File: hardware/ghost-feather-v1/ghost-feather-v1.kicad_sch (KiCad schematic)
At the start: 41 parts, among them J1 Conn_ARM_SWD_TagConnect_TC2030, J2 USB_C_Receptacle_USB2.0, J3 Conn_01x03, J4 Conn_01x03, J5 Conn_01x03, J6 Conn_01x03, SW2 BOOT0, U1 STM32F722RETx, U2 BMI270, U3 USBLC6-2SC6_MOD, U4 ADP2108AUJ-3.3, U5 LM2596S-5, X2 32kHz768

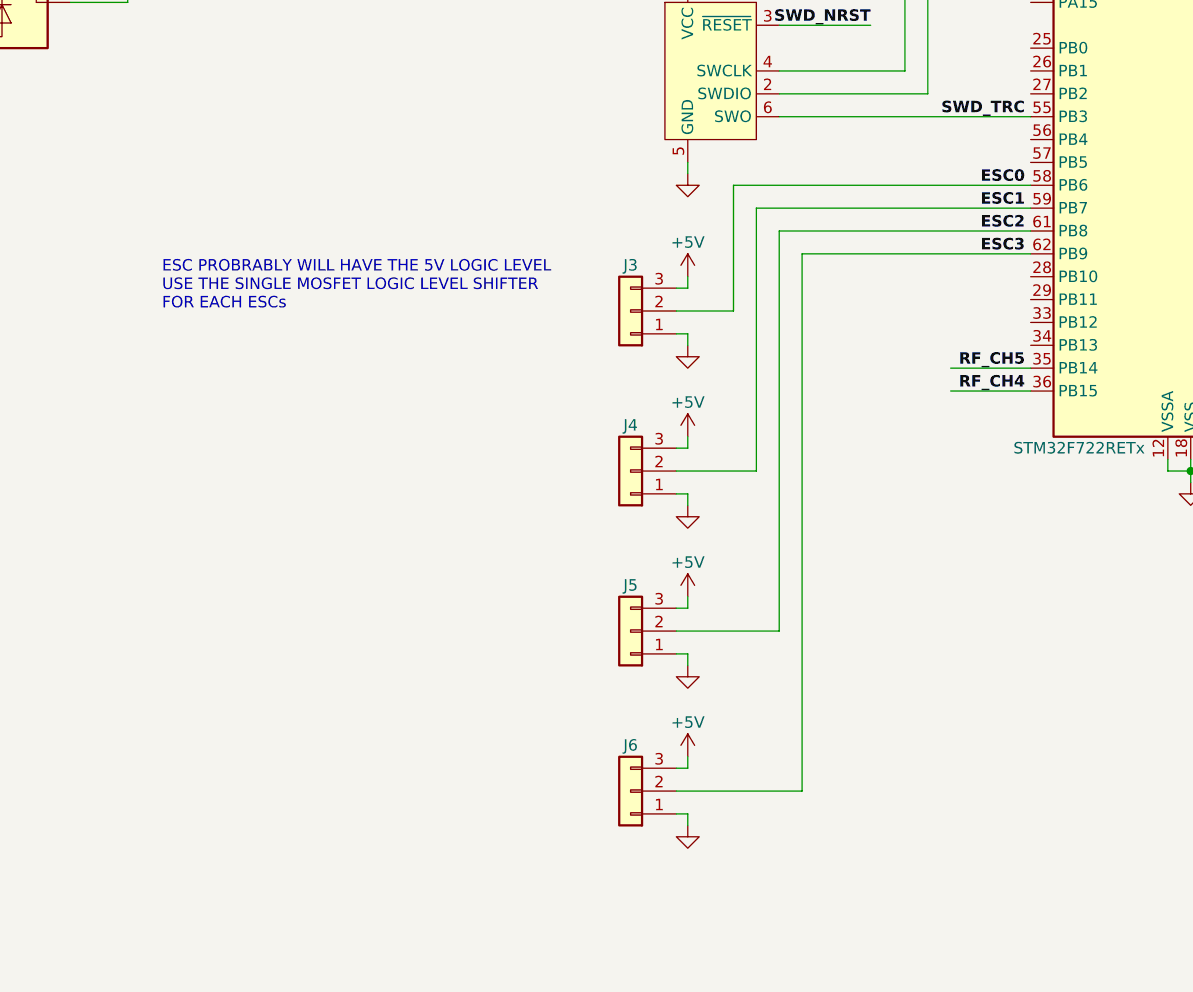
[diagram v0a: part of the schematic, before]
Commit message: feat: Add the MOSFET logic level shifters for every ESC
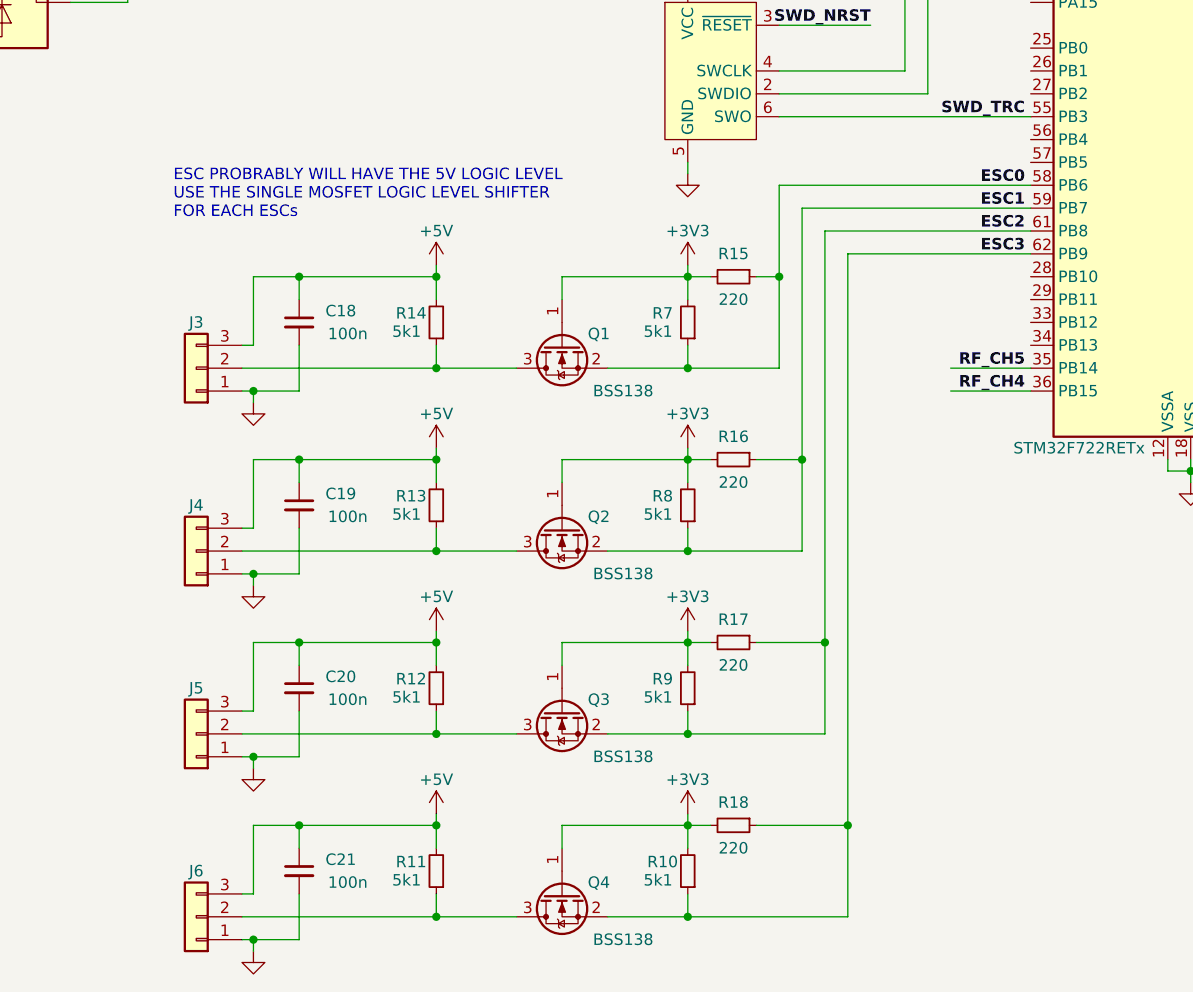
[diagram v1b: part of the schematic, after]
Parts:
- added C18, C19, C20, C21: 100n, symbol Device:C_Small
- added Q1, Q2, Q3, Q4: BSS138, Package_TO_SOT_SMD:SOT-23, symbol Transistor_FET:BSS138
- added R10, R11, R12, R13, R14, R7, R8, R9: 5k1, symbol Device:R_Small
- added R15, R16, R17, R18: 220, symbol Device:R_Small
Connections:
- net +3V3: now also Q1.1 (G), Q2.1 (G), Q3.1 (G), Q4.1 (G), R10.2, R15.2, R16.2, R17.2, R18.2, R7.2, R8.2, R9.2
- net +5V: now also C18.1, C19.1, C20.1, C21.1, R11.2, R12.2, R13.2, R14.2
- net ESC0: now also Q1.2 (S), R15.1, R7.1; no longer J3.2 (Pin_2)
- net ESC1: now also Q2.2 (S), R16.1, R8.1; no longer J4.2 (Pin_2)
- net ESC2: now also Q3.2 (S), R17.1, R9.1; no longer J5.2 (Pin_2)
- net ESC3: now also Q4.2 (S), R10.1, R18.1; no longer J6.2 (Pin_2)
- net GND: now also C18.2, C19.2, C20.2, C21.2
- new net: J5.2 (Pin_2), Q3.3 (D), R12.1
- new net: J3.2 (Pin_2), Q1.3 (D), R14.1
- new net: J4.2 (Pin_2), Q2.3 (D), R13.1
- new net: J6.2 (Pin_2), Q4.3 (D), R11.1
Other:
- moved on the sheet: J3, J4, J5, J6

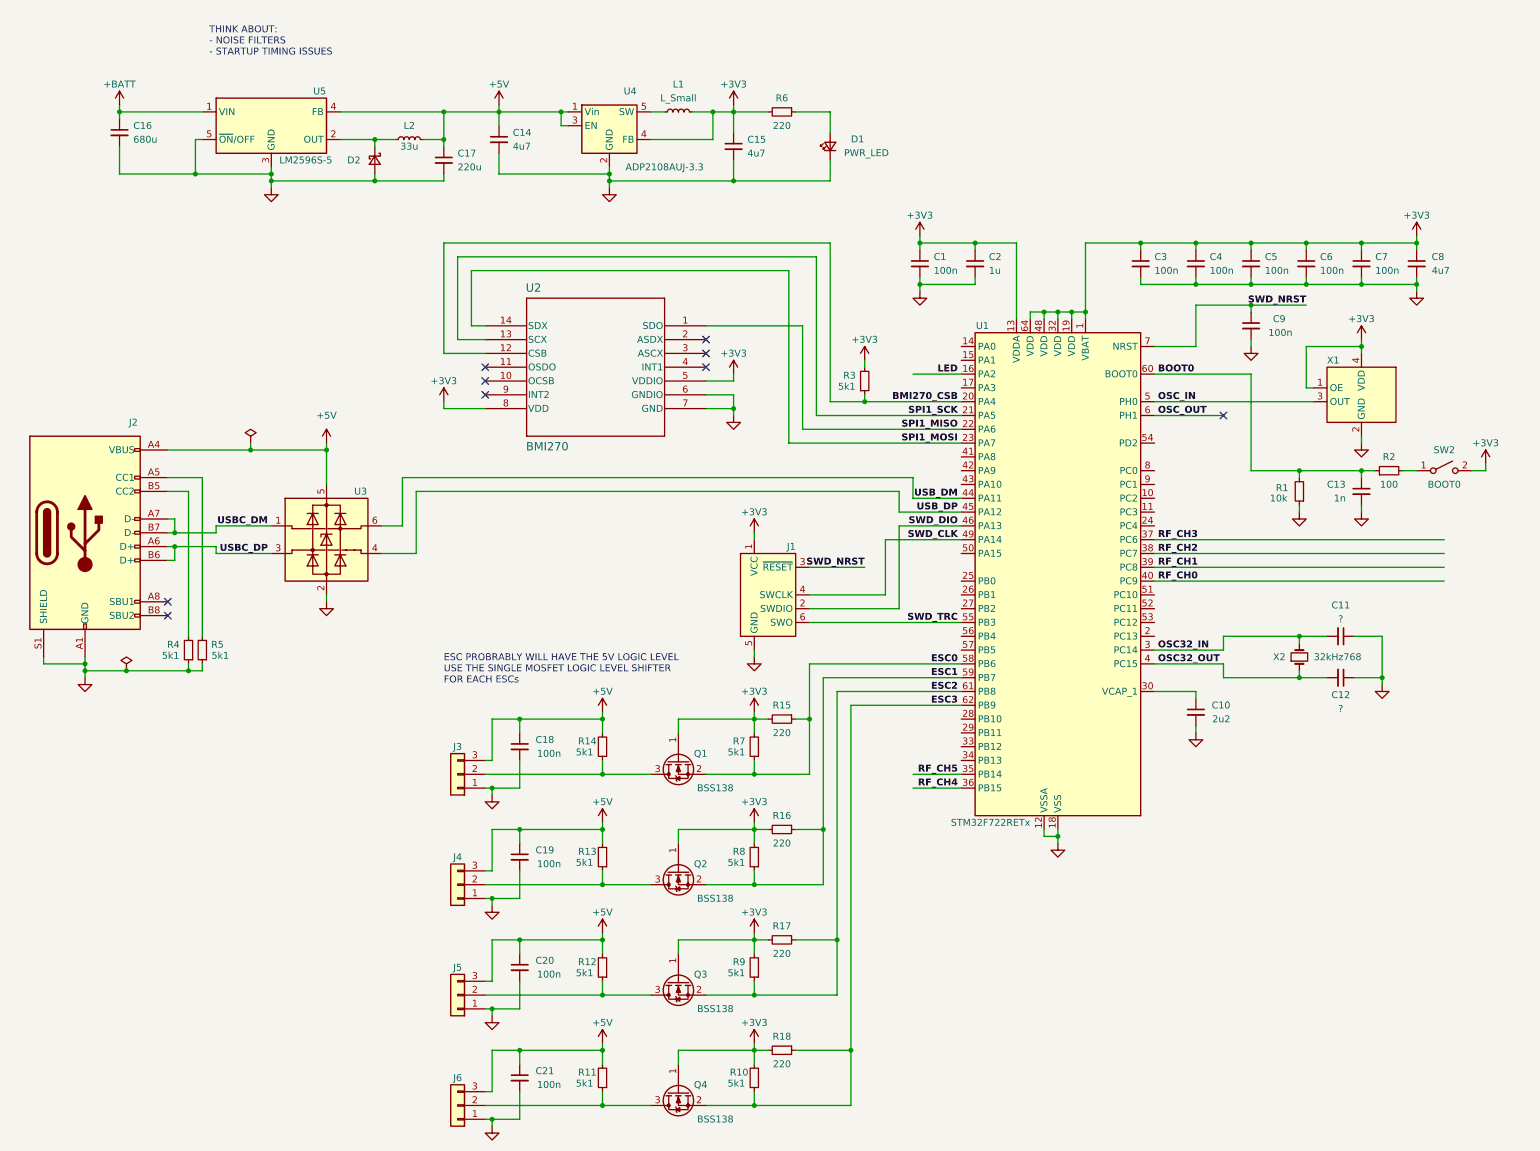
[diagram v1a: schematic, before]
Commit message: feat: Add RF channel connector. Start adding the parts information
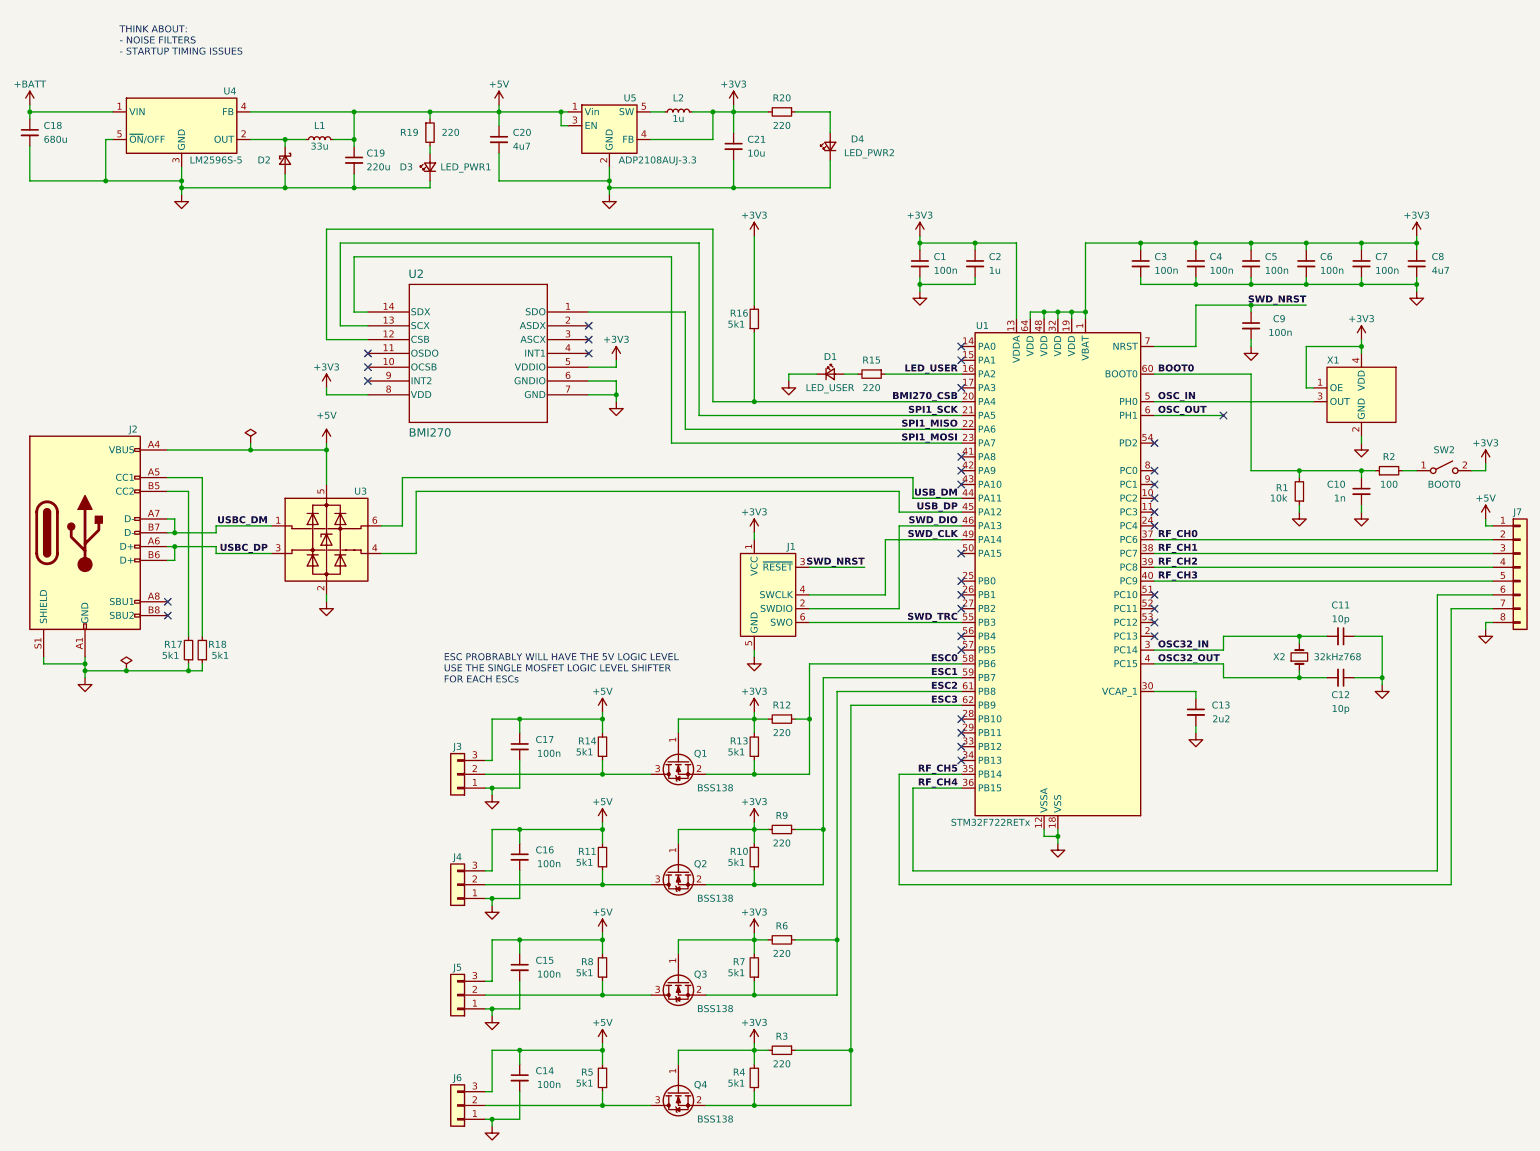
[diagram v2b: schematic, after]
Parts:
- removed R3: 5k1, symbol Device:R_Small
- added D1: LED_USER, symbol Device:LED_Small
- added D3: LED_PWR1, symbol Device:LED_Small
- added J7: Conn_01x08, symbol Connector_Generic:Conn_01x08
- added R15, R19: 220, symbol Device:R_Small
- added R16: 5k1, symbol Device:R_Small
- C11, C12: value ? -> 10p
- C21: renamed from C15; value 4u7 -> 10u
- D4: renamed from D1; value PWR_LED -> LED_PWR2
- L2: renamed from L1; value L_Small -> 1u
- U1: Distributor Link (none) -> https://eu.mouser.com/ProductDetail/STMicroelectronics/STM3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; Manufacturer (none) -> STMicroelectronics; Manufacturer Part Number (none) -> STM32F722RET6
- U2: Distributor Link (none) -> https://eu.mouser.com/ProductDetail/Bosch-Sensortec/BMI270?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; Manufacturer (none) -> Bosch Sensortec; Manufacturer Part Number (none) -> BMI270
- U3: Distributor Link (none) -> https://eu.mouser.com/ProductDetail/STMicroelectronics/USBL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; Manufacturer (none) -> STMicroelectronics; Manufacturer Part Number (none) -> USBLC6-2SC6
- U4: renamed from U5; Distributor Link (none) -> https://eu.mouser.com/ProductDetail/Texas-Instruments/LM259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; Manufacturer (none) -> Texas Instruments; Manufacturer Part Number (none) -> LM2596S-5.0/NOPB
- U5: renamed from U4; Distributor Link (none) -> https://eu.mouser.com/ProductDetail/Analog-Devices/ADP2108A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; Manufacturer (none) -> Analog Devices; Manufacturer Part Number (none) -> ADP2108AUJZ-3.3-R7
- X1: Distributor Link (none) -> https://eu.mouser.com/ProductDetail/ABRACON/AMPMGFB-16.0000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; Manufacturer (none) -> ABRACON; Manufacturer Part Number (none) -> AMPMGFB-16.0000T
- X2: Distributor Link (none) -> https://eu.mouser.com/ProductDetail/Micro-Crystal/CC4V-T1A-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; Manufacturer (none) -> Micro Crystal; Manufacturer Part Number (none) -> CC4V-T1A-32.768kHz-10pF-20PPM-TA-QC
- renumbered C13 to C10, C10 to C13, C21 to C14, C20 to C15, C19 to C16, C18 to C17, C16 to C18, C17 to C19, C14 to C20, L2 to L1, R8 to R10, R13 to R11, R15 to R12, R7 to R13, R4 to R17, R5 to R18, R6 to R20, R18 to R3, R10 to R4, R11 to R5, R17 to R6, R9 to R7, R12 to R8, R16 to R9
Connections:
- net +3V3: now also R16.2
- net +5V: now also J7.1 (Pin_1), R19.1
- net BMI270_CSB: now also R16.1
- net GND: now also D1.1 (K), D3.1 (K), J7.8 (Pin_8)
- net RF_CH0: now also U1.37 (PC6), J7.2 (Pin_2); no longer U1.40 (PC9)
- net RF_CH1: now also U1.38 (PC7), J7.3 (Pin_3); no longer U1.39 (PC8)
- net RF_CH2: now also U1.39 (PC8), J7.4 (Pin_4); no longer U1.38 (PC7)
- net RF_CH3: now also U1.40 (PC9), J7.5 (Pin_5); no longer U1.37 (PC6)
- net RF_CH4: now also J7.6 (Pin_6)
- net RF_CH5: now also J7.7 (Pin_7)
- net LED renamed LED_USER
- net LED_USER: now also R15.1
- new net: D3.2 (A), R19.2
- new net: D1.2 (A), R15.2
- no-connect marks 9 -> 35
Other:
- moved on the sheet: C18, C19, D2, L1, U2, U4
